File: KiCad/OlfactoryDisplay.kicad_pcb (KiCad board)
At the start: 2 copper layers, 48 x 39.5 mm, 16 parts, among them J1 B2B-PH-K-S, J2 B2B-PH-K-S, J3 B2B-PH-K-S, J4 B2B-PH-K-S, J5 B2B-PH-K-S, J6 B2B-PH-K-S, J7 B2B-PH-K-S, J9 B2B-PH-K-S, U1 DMG1012UW-7, U2 DMG1012UW-7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

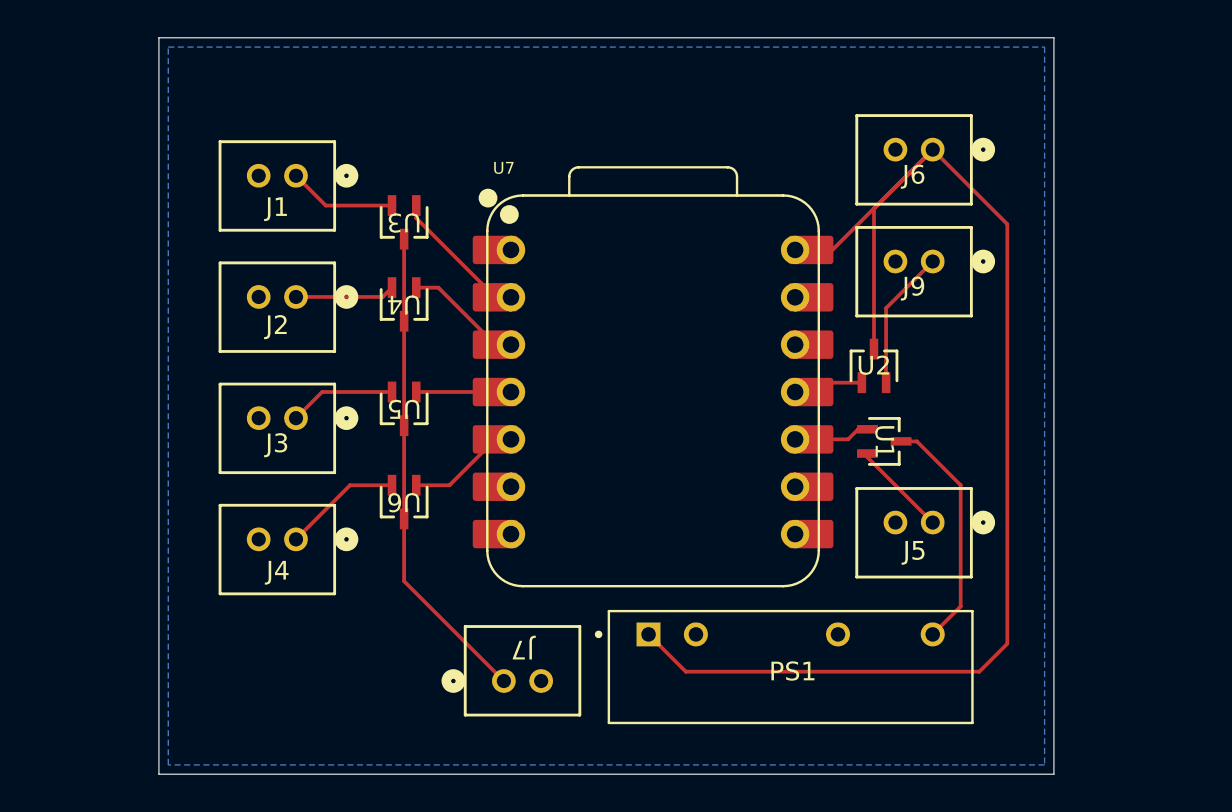
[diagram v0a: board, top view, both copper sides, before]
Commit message: added CUXR logo to the pcb
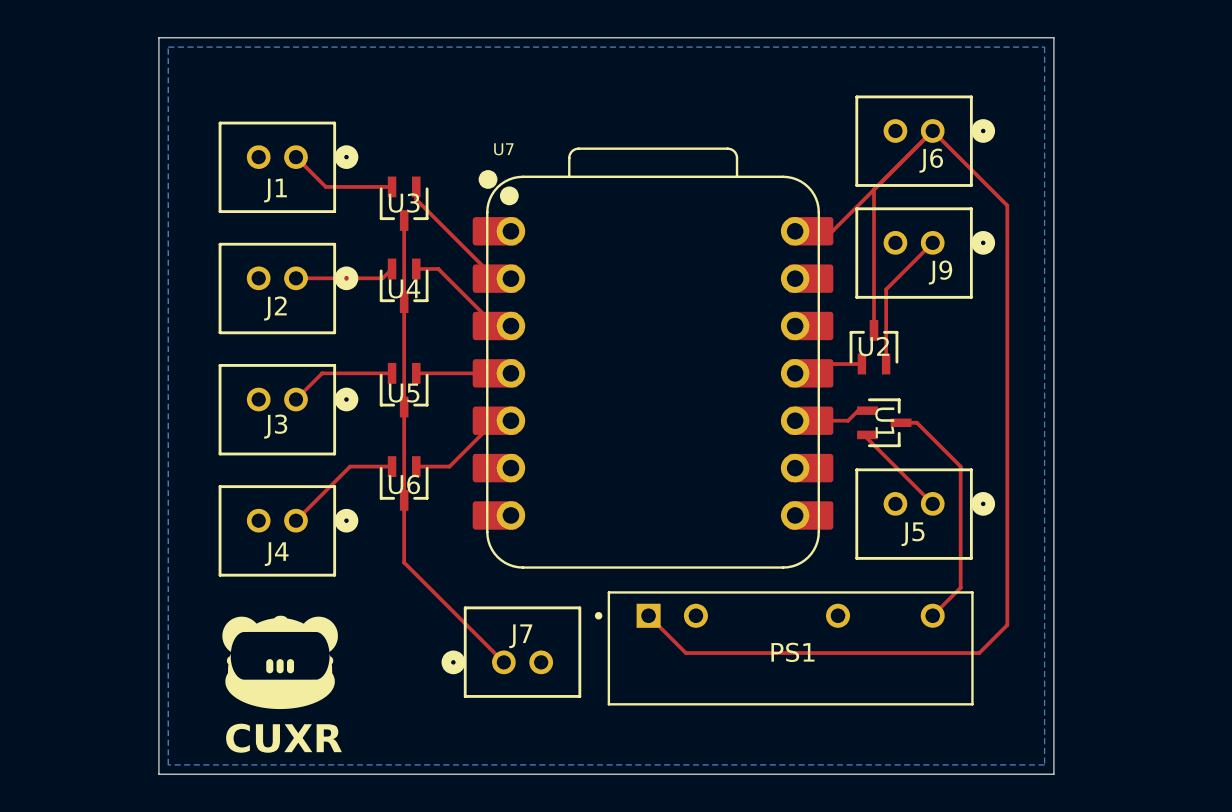
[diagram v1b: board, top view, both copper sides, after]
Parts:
- added G***: LOGO, LOGO, F.Cu at (84.0, 83.0)
- moved J1 1.00 mm to (84.9, 55.9)
- moved J2 1.00 mm to (84.9, 62.4)
- moved J3 1.00 mm to (84.9, 68.9)
- moved J4 1.00 mm to (84.9, 75.4)
- moved J5 1.00 mm to (119.0, 74.5)
- moved J6 1.00 mm to (119.0, 54.5)
- moved J7 1.00 mm to (96.0, 83.0)
- moved J9 1.00 mm to (119.0, 60.5)
- moved PS1 1.00 mm to (111.4, 82.2)
- moved U1 1.00 mm to (116.4, 70.1)
- moved U2 1.00 mm to (115.9, 66.1)
- moved U3 1.00 mm to (90.6, 58.4)
- moved U4 1.00 mm to (90.6, 62.8)
- moved U5 1.00 mm to (90.6, 68.4)
- moved U6 1.00 mm to (90.6, 73.4)
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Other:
- board text added: "CUXR"

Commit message: updated pdb thing
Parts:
- removed G***: LOGO, LOGO
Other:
- board text removed: "CUXR"

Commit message: Final Version of V1 with Logo Included
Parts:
- added G***: LOGO, Custom:CUXR_Logo_Halftone, F.Cu at (86.0, 82.0)
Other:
- board size 48 x 39.5 mm -> 44 x 34.5 mm
- board text added: "CUXR - OLFACTORY V1"
- board text added: "ERIC SEO - eys39"
- board text added: "ZACH RIIFF - zcr5"

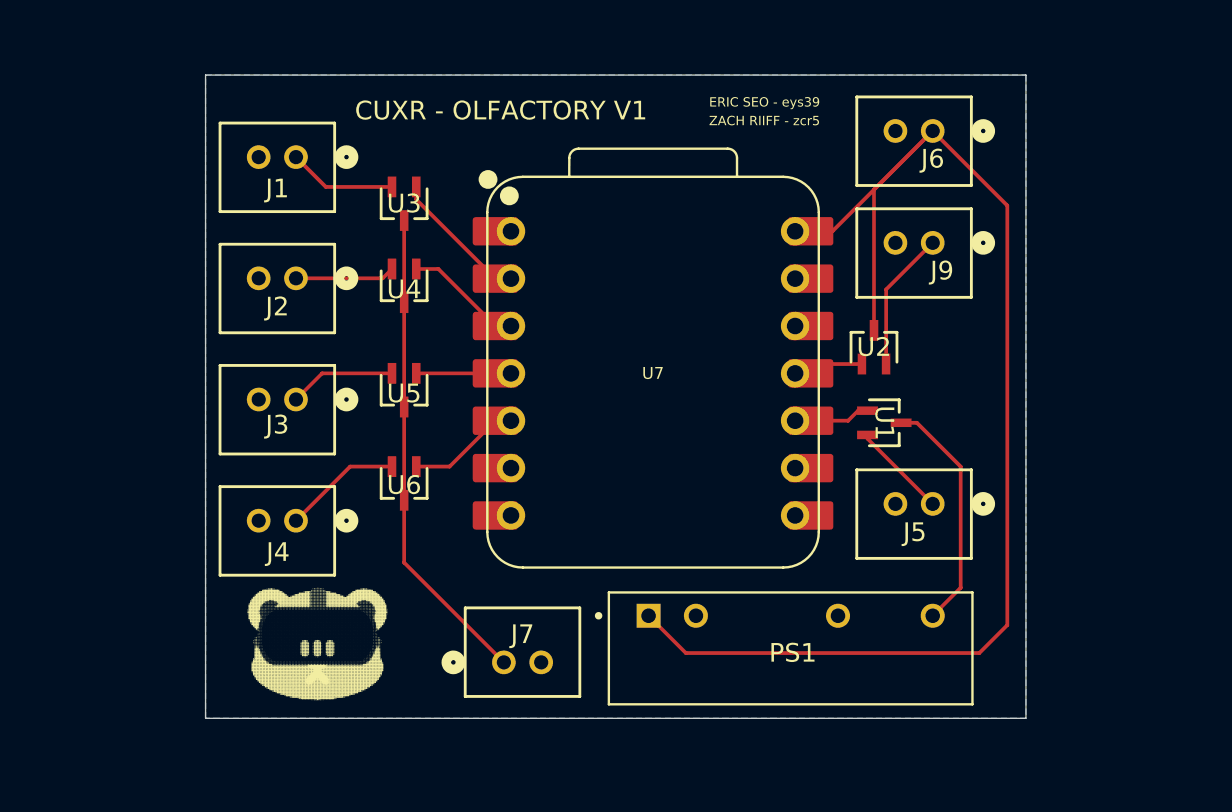
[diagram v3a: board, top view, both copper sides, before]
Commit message: Updated Gerber files. Moved text around.
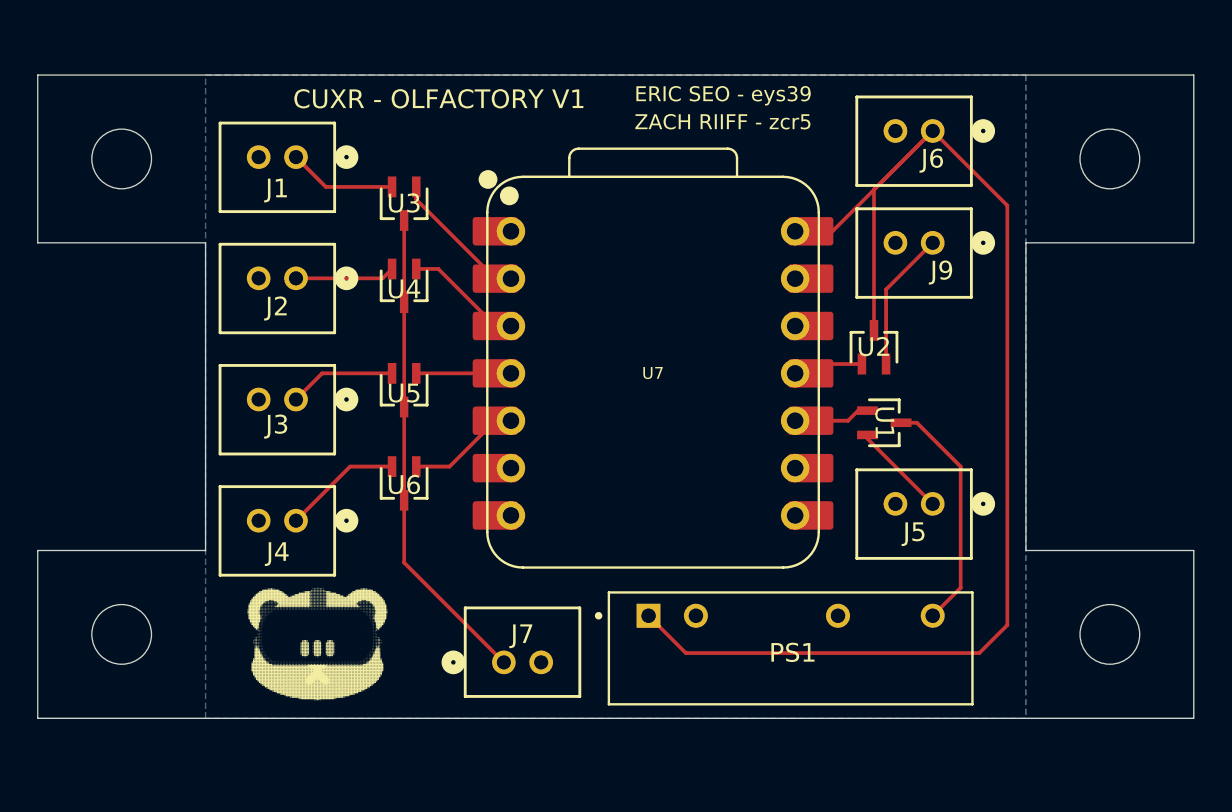
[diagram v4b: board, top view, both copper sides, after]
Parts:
- added REF**: MountingHole_3.2mm_M3, MountingHole:MountingHole_3.2mm_M3, F.Cu at (75.5, 81.5)
- added REF**: MountingHole_3.2mm_M3, MountingHole:MountingHole_3.2mm_M3, F.Cu at (128.5, 81.5)
- added REF**: MountingHole_3.2mm_M3, MountingHole:MountingHole_3.2mm_M3, F.Cu at (75.5, 56.0)
- added REF**: MountingHole_3.2mm_M3, MountingHole:MountingHole_3.2mm_M3, F.Cu at (128.5, 56.0)
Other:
- board size 44 x 34.5 mm -> 62 x 34.5 mm
